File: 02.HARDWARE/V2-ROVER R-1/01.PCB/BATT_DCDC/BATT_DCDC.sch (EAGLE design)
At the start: 60 parts, among them J1 DF40C-20DP-0.4V_51_, K1 FLEX11, Q1 NVTFS9D6P04M8LTAG, Q2 2N7002PW, U1 MCP6071T-E/OT, U2 LM5114BMF_NOPB, U3 TPS55330RTET, U7 MCP6071T-E/OT

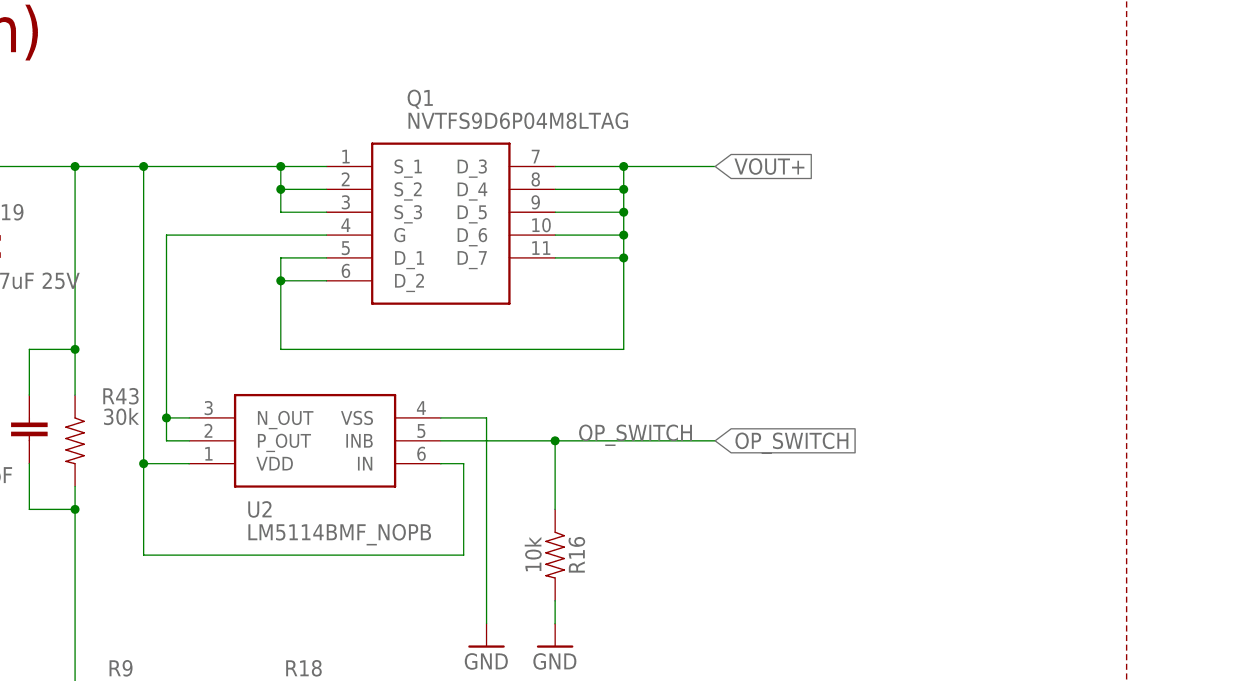
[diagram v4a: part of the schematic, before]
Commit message: Modificacion DCDC y Conector
DCDC: Posible version exclusiva PMU
Conector: Adatacion a cambio en produccion de un componente (SMJ)
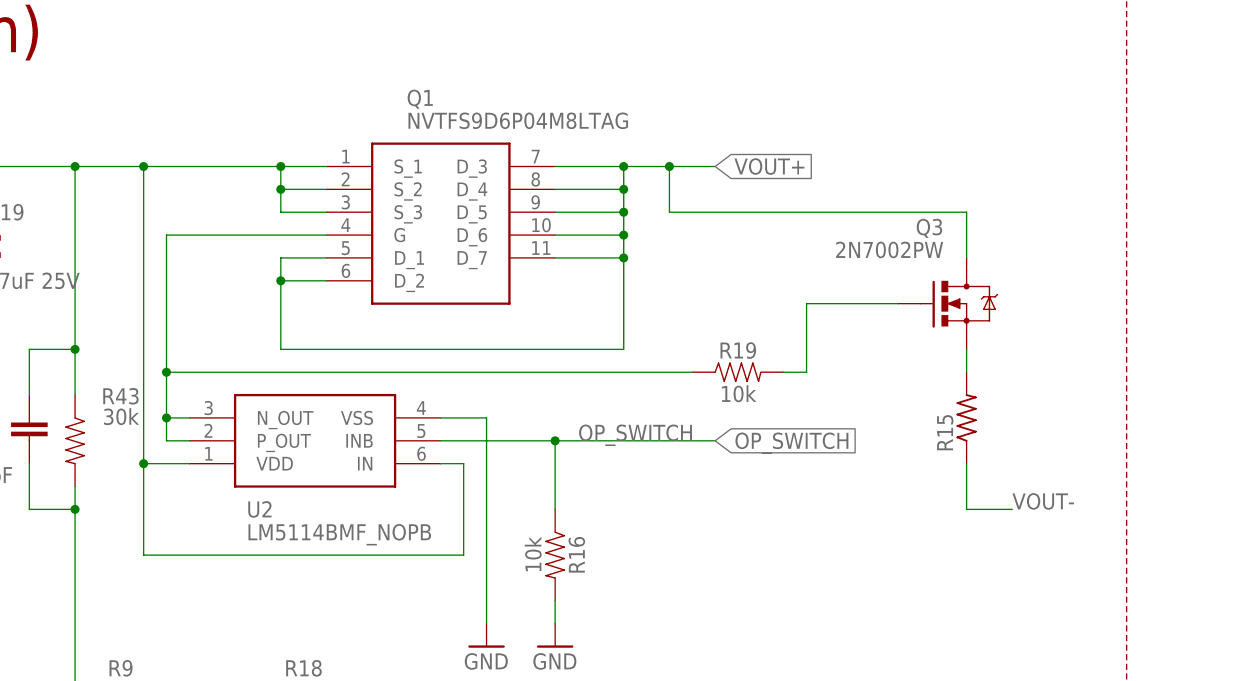
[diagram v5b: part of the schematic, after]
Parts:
- added Q3: 2N7002PW, SparkFun-DiscreteSemi:MOSFET-NCHANNEL2N7002PW
- added R15: (no value), adafruit:R-US_R2512
- added R19: 10k, SparkFun-Resistors:RESISTOR0402
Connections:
- new net N$13: Q3.G, R19.2
- new net N$8: Q3.S, R15.2
- net N$9: now also R19.1
- net VOUT+: now also Q3.D
- net VOUT-: now also R15.1
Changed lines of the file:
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@@
 <part name="U2" library="LM5114BMF_NOPB" deviceset="LM5114BMF_NOPB" device=""/>
 <part name="GND2" library="SparkFun" deviceset="GND" device=""/>
+<part name="R15" library="adafruit" library_urn="urn:adsk.eagle:library:420" deviceset="R-US_" device="R2512" package3d_urn="urn:adsk.eagle:package:6240577/1"/>
+<part name="Q3" library="SparkFun-DiscreteSemi" deviceset="MOSFET-NCHANNEL" device="2N7002PW" value="2N7002PW"/>
+<part name="R19" library="SparkFun-Resistors" library_urn="urn:adsk.eagle:library:532" deviceset="RESISTOR" device="0402" package3d_urn="urn:adsk.eagle:package:39657/1" value="10k"/>
 </parts>
 <sheets>
@@
 <instance part="GND2" gate="1" x="215.9" y="175.26" smashed="yes">
 <attribute name="VALUE" x="213.36" y="172.72" size="1.778" layer="96"/>
+</instance>
+<instance part="R15" gate="G$1" x="269.24" y="200.66" smashed="yes" rot="R90">
+<attribute name="NAME" x="267.7414" y="196.85" size="1.778" layer="95" rot="R90"/>
+<attribute name="VALUE" x="272.542" y="196.85" size="1.778" layer="96" rot="R90"/>
+</instance>
+<instance part="Q3" gate="G$1" x="269.24" y="213.36" smashed="yes">
+<attribute name="NAME" x="266.7" y="220.98" size="1.778" layer="95" rot="MR0"/>
+<attribute name="VALUE" x="266.7" y="218.44" size="1.778" layer="96" rot="MR0"/>
+</instance>
+<instance part="R19" gate="G$1" x="243.84" y="205.74" smashed="yes">
+<attribute name="NAME" x="243.84" y="207.264" size="1.778" layer="95" font="vector" align="bottom-center"/>
+<attribute name="VALUE" x="243.84" y="204.216" size="1.778" layer="96" font="vector" align="top-center"/>
 </instance>
 </instances>
@@
 <junction x="231.14" y="218.44"/>
 <label x="241.3" y="228.6" size="1.778" layer="95" xref="yes"/>
-<wire x1="231.14" y1="228.6" x2="241.3" y2="228.6" width="0.1524" layer="91"/>
+<wire x1="231.14" y1="228.6" x2="236.22" y2="228.6" width="0.1524" layer="91"/>
 <junction x="231.14" y="228.6"/>
+<wire x1="236.22" y1="228.6" x2="241.3" y2="228.6" width="0.1524" layer="91"/>
+<wire x1="236.22" y1="223.52" x2="236.22" y2="228.6" width="0.1524" layer="91"/>
+<junction x="236.22" y="228.6"/>
+<pinref part="Q3" gate="G$1" pin="D"/>
+<wire x1="269.24" y1="218.44" x2="269.24" y2="223.52" width="0.1524" layer="91"/>
+<wire x1="269.24" y1="223.52" x2="236.22" y2="223.52" width="0.1524" layer="91"/>
 </segment>
 <segment>
@@
 <label x="345.44" y="53.34" size="1.778" layer="95"/>
 <pinref part="K1" gate="G$1" pin="P$10"/>
+</segment>
+<segment>
+<pinref part="R15" gate="G$1" pin="1"/>
+<wire x1="269.24" y1="195.58" x2="269.24" y2="190.5" width="0.1524" layer="91"/>
+<wire x1="269.24" y1="190.5" x2="274.32" y2="190.5" width="0.1524" layer="91"/>
+<label x="274.32" y="190.5" size="1.778" layer="95"/>
 </segment>
 </net>
@@
 <pinref part="U2" gate="G$1" pin="N_OUT"/>
 <wire x1="182.88" y1="200.66" x2="180.34" y2="200.66" width="0.1524" layer="91"/>
-<wire x1="180.34" y1="200.66" x2="180.34" y2="220.98" width="0.1524" layer="91"/>
 <pinref part="Q1" gate="G$1" pin="G"/>
+<wire x1="180.34" y1="200.66" x2="180.34" y2="205.74" width="0.1524" layer="91"/>
+<wire x1="180.34" y1="205.74" x2="180.34" y2="220.98" width="0.1524" layer="91"/>
 <wire x1="180.34" y1="220.98" x2="198.12" y2="220.98" width="0.1524" layer="91"/>
 <wire x1="180.34" y1="200.66" x2="180.34" y2="198.12" width="0.1524" layer="91"/>
 <junction x="180.34" y="200.66"/>
 <wire x1="180.34" y1="198.12" x2="182.88" y2="198.12" width="0.1524" layer="91"/>
-</segment>
-</net>
+<pinref part="R19" gate="G$1" pin="1"/>
+<wire x1="180.34" y1="205.74" x2="238.76" y2="205.74" width="0.1524" layer="91"/>
+<junction x="180.34" y="205.74"/>
+</segment>
+</net>
+<net name="N$8" class="0">
+<segment>
+<pinref part="R15" gate="G$1" pin="2"/>
+<wire x1="269.24" y1="205.74" x2="269.24" y2="208.28" width="0.1524" layer="91"/>
+<pinref part="Q3" gate="G$1" pin="S"/>
+</segment>
+</net>
+<net name="N$13" class="0">
+<segment>
+<pinref part="Q3" gate="G$1" pin="G"/>
+<wire x1="251.46" y1="213.36" x2="261.62" y2="213.36" width="0.1524" layer="91"/>
+<wire x1="251.46" y1="205.74" x2="251.46" y2="213.36" width="0.1524" layer="91"/>
+<pinref part="R19" gate="G$1" pin="2"/>
+<wire x1="248.92" y1="205.74" x2="251.46" y2="205.74" width="0.1524" layer="91"/>
+</segment>
+</net>
